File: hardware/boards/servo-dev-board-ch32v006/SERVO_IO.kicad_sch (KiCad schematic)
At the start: 7 parts, among them J4 JST-ZH-H, J5 PIN-V, J6 PIN-V

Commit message: updated LCSC part numbers for all symbols
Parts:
- C14: LCSC C307331 -> C28233
- J4: LCSC (none) -> C265404
- J5: LCSC (none) -> C42431812
- J6: LCSC C485354 -> C66690
- R12: LCSC C25744 -> C17414
- R13: LCSC C25900 -> C17673
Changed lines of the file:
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@@
 			)
 		)
-		(property "LCSC" "C25744"
+		(property "LCSC" "C17414"
 			(at 23.876 85.852 0)
 			(effects
@@
 			)
 		)
+		(property "LCSC" "C265404"
+			(at 43.18 39.37 0)
+			(effects
+				(font
+					(size 1.27 1.27)
+				)
+				(hide yes)
+			)
+		)
 		(pin "3"
 		)
@@
 			)
 		)
-		(property "LCSC" "C307331"
+		(property "LCSC" "C28233"
 			(at 70.866 97.536 0)
 			(effects
@@
 			)
 		)
-		(property "LCSC" "C25900"
+		(property "LCSC" "C17673"
 			(at 64.516 87.63 0)
 			(effects
@@
 			)
 		)
-		(property "LCSC" "C485354"
+		(property "LCSC" "C66690"
 			(at 147.32 40.64 0)
 			(effects
@@
 			(effects
 				(font
+					(size 1.27 1.27)
+				)
+				(hide yes)
+			)
+		)
+		(property "LCSC" "C42431812"
+			(at 96.52 40.64 0)
+			(effects
+				(font

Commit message: remove 'LCSC Part' Property from project
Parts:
- J4: LCSC Part C265404 -> (none)
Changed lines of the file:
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@@
-			)
-		)
-		(property "LCSC Part" "C265404"
-			(at 43.18 68.58 0)
-			(effects
-				(font
-					(size 1.27 1.27)
-				)
-				(hide yes)
 			)
 		)

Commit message: added MFPN properties
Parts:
- C14: MFPN (none) -> CL21B104KCFNNNE
- J4: MFPN (none) -> S5B-ZR(LF)(SN)
- J5: MFPN (none) -> PZ2.54-1X5P-H25
- J6: MFPN (none) -> 2.54-2*2P
- R12: MFPN (none) -> 0805W8F1002T5E
- R13: MFPN (none) -> 0805W8F4701T5E
- TH1: MFPN (none) -> SDNT2012X103F3950FTF
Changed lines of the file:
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@@
+			)
+		)
+		(property "MFPN" "0805W8F1002T5E"
+			(at 23.876 85.852 0)
+			(effects
+				(font
+					(size 1.27 1.27)
+				)
+				(hide yes)
 			)
 		)
@@
 			)
 		)
+		(property "MFPN" "S5B-ZR(LF)(SN)"
+			(at 43.18 39.37 0)
+			(effects
+				(font
+					(size 1.27 1.27)
+				)
+				(hide yes)
+			)
+		)
 		(pin "3"
 		)
@@
 			)
 		)
+		(property "MFPN" "CL21B104KCFNNNE"
+			(at 70.866 97.536 0)
+			(effects
+				(font
+					(size 1.27 1.27)
+				)
+				(hide yes)
+			)
+		)
 		(pin "1"
 		)
@@
 			)
 		)
+		(property "MFPN" "0805W8F4701T5E"
+			(at 64.516 87.63 0)
+			(effects
+				(font
+					(size 1.27 1.27)
+				)
+				(hide yes)
+			)
+		)
 		(pin "1"
 		)
@@
 			)
 		)
+		(property "MFPN" "SDNT2012X103F3950FTF"
+			(at 31.75 97.7899 0)
+			(effects
+				(font
+					(size 1.27 1.27)
+				)
+				(hide yes)
+			)
+		)
 		(pin "2"
 		)
@@
 			)
 		)
+		(property "MFPN" "2.54-2*2P"
+			(at 147.32 40.64 0)
+			(effects
+				(font
+					(size 1.27 1.27)
+				)
+				(hide yes)
+			)
+		)
 		(pin "4"
 		)
@@
 			(at 96.52 40.64 0)
 			(effects
+				(font
+					(size 1.27 1.27)
+				)
+				(hide yes)
+			)
+		)
+		(property "MFPN" "PZ2.54-1X5P-H25"
+			(at 96.52 40.64 0)
+			(effects

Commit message: update board
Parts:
- removed R12: 10kΩ, Resistor_SMD:R_0805_2012Metric_Pad1.20x1.40mm_HandSolder, symbol Device:R
- added J5: NTC EXT, symbol Connector_Generic:Conn_01x02
- added JP1: Jumper_3_Open, symbol Jumper:Jumper_3_Open
- added R13: 10kΩ, Resistor_SMD:R_0805_2012Metric_Pad1.20x1.40mm_HandSolder, symbol Device:R
- renumbered C14 to C11, J5 to J6, J6 to J7, R13 to R14
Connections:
- net +3V3: now also R13.1
- net GND: now also J5.2 (Pin_2)
- net VNTC: now also JP1.2 (C), R13.2; no longer TH1.1
- new net: J5.1 (Pin_1), JP1.1 (A)
- new net: JP1.3 (B), TH1.1
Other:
- moved on the sheet: C11, R14, TH1

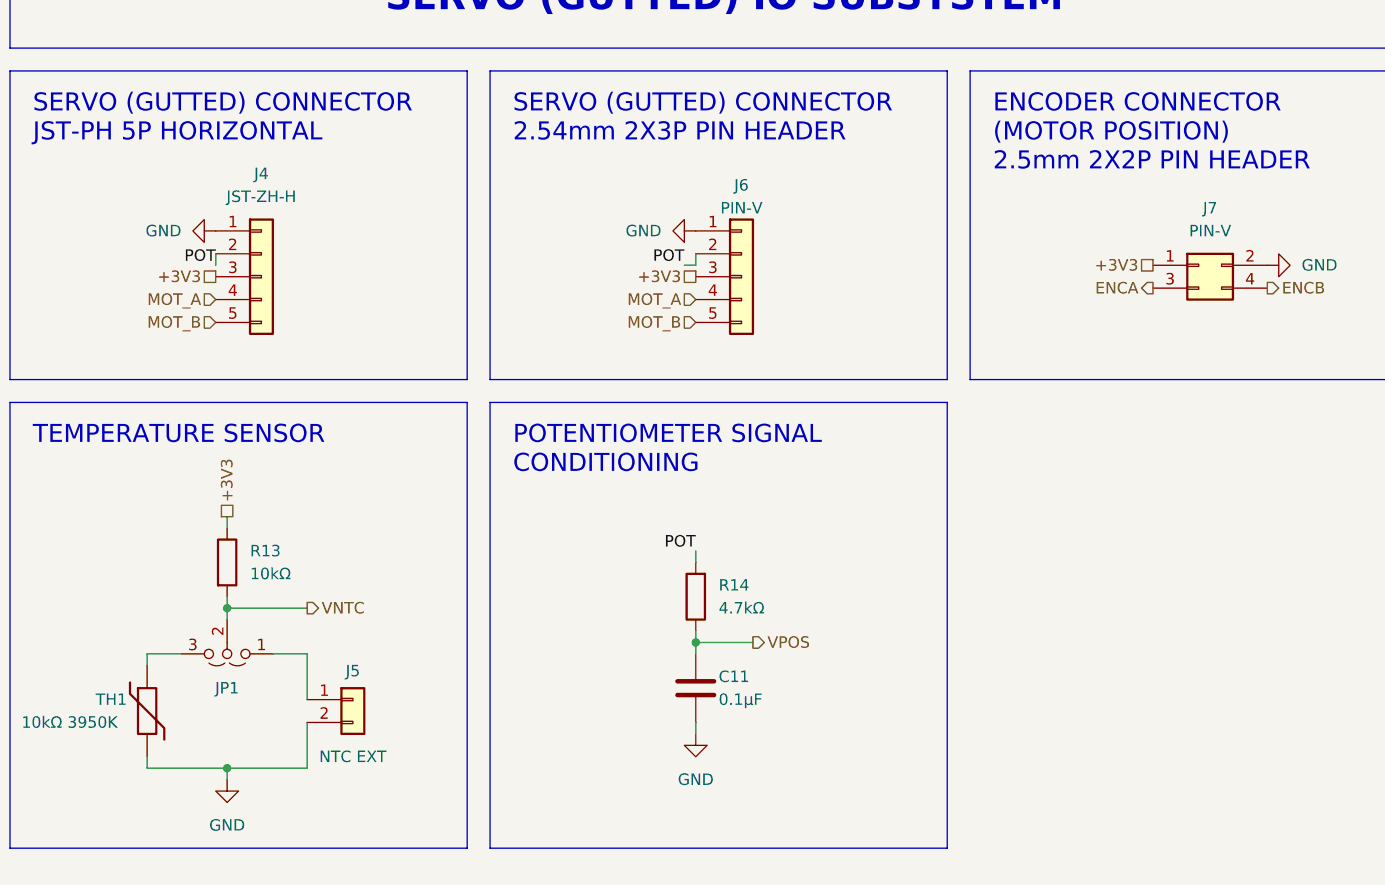
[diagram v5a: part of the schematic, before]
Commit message: updated schematics. ERC on schematics is now passing
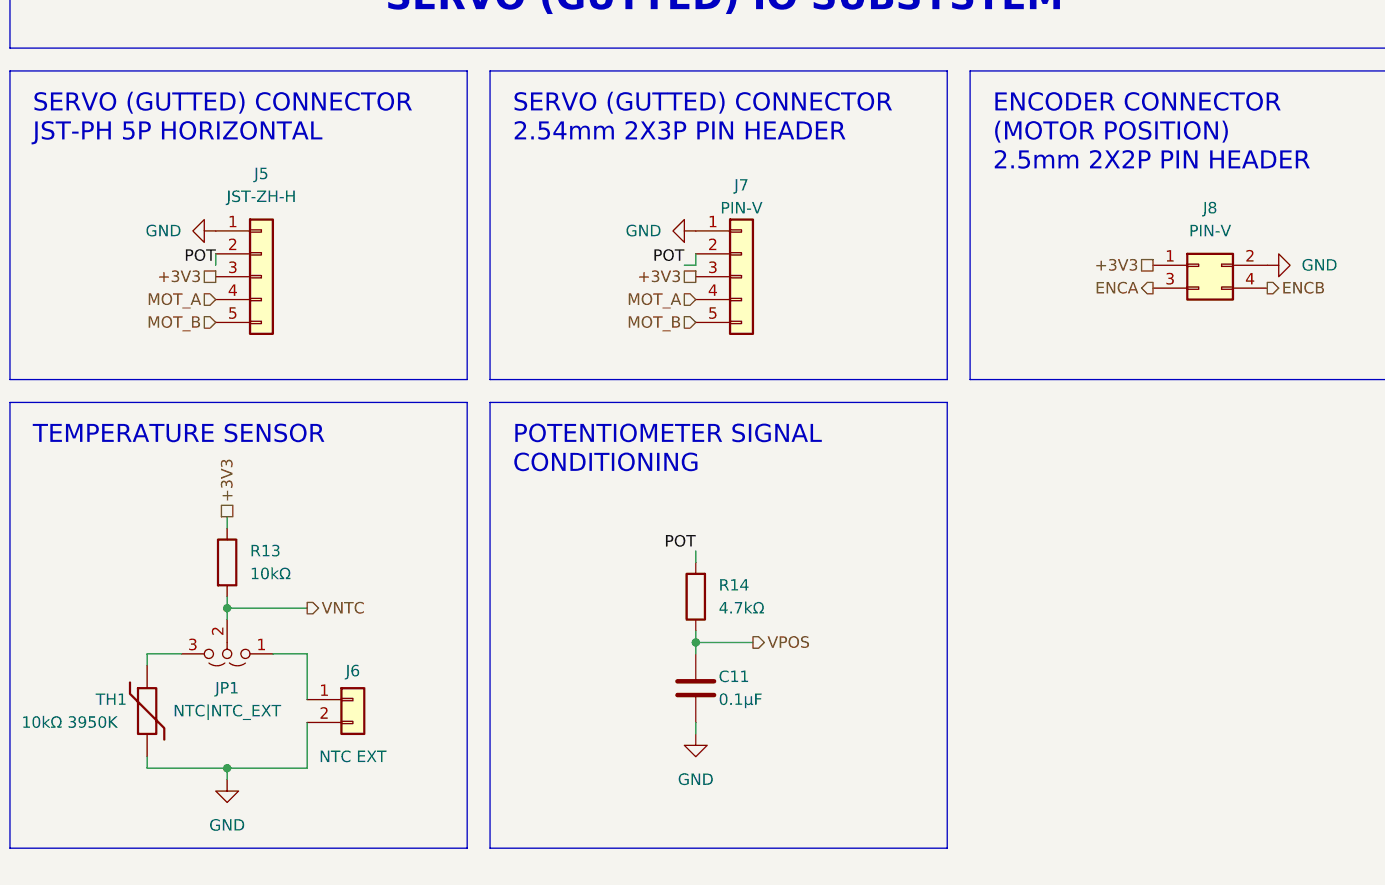
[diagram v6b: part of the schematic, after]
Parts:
- J6: renamed from J5; footprint (none) -> Connector_PinHeader_2.54mm:PinHeader_1x02_P2.54mm_Vertical
- JP1: value Jumper_3_Open -> NTC|NTC_EXT; footprint (none) -> Connector_PinHeader_2.54mm:PinHeader_1x03_P2.54mm_Vertical
- renumbered J4 to J5, J6 to J7, J7 to J8
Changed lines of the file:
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@@
 			)
 		)
-		(property "Value" "Jumper_3_Open"
+		(property "Value" "NTC|NTC_EXT"
 			(at 39.37 99.06 0)
-			(hide yes)
-			(show_name no)
-			(do_not_autoplace no)
-			(effects
-				(font
-					(size 1.27 1.27)
-				)
-			)
-		)
-		(property "Footprint" ""
+			(show_name no)
+			(do_not_autoplace no)
+			(effects
+				(font
+					(size 1.27 1.27)
+				)
+			)
+		)
+		(property "Footprint" "Connector_PinHeader_2.54mm:PinHeader_1x03_P2.54mm_Vertical"
 			(at 39.37 92.71 0)
 			(hide yes)
@@
 		(dnp no)
 		(fields_autoplaced yes)
-		(property "Reference" "#PWR040"
+		(property "Reference" "#PWR046"
 			(at 91.44 107.95 0)
 			(hide yes)
@@
 			(project "servo-dev-board-ch32v006"
 				(path "/6062e7d2-0c72-467e-b49c-6387ba053e09/120e2627-930f-4b00-8e4a-c64cf3d97f18"
-					(reference "#PWR040")
+					(reference "#PWR046")
 					(unit 1)
 				)
@@
 		(in_pos_files yes)
 		(dnp no)
-		(property "Reference" "J4"
+		(property "Reference" "J5"
 			(at 43.18 39.37 0)
 			(show_name no)
@@
 			(project "servo-dev-board-ch32v006"
 				(path "/6062e7d2-0c72-467e-b49c-6387ba053e09/120e2627-930f-4b00-8e4a-c64cf3d97f18"
-					(reference "J4")
+					(reference "J5")
 					(unit 1)
 				)
@@
 		(dnp no)
 		(fields_autoplaced yes)
-		(property "Reference" "#PWR041"
+		(property "Reference" "#PWR047"
 			(at 161.29 49.53 0)
 			(hide yes)
@@
 			(project "servo-dev-board-ch32v006"
 				(path "/6062e7d2-0c72-467e-b49c-6387ba053e09/120e2627-930f-4b00-8e4a-c64cf3d97f18"
-					(reference "#PWR041")
+					(reference "#PWR047")
 					(unit 1)
 				)
@@
 		(dnp no)
 		(fields_autoplaced yes)
-		(property "Reference" "#PWR039"
+		(property "Reference" "#PWR045"
 			(at 85.09 45.72 0)
 			(hide yes)
@@
 			(project "servo-dev-board-ch32v006"
 				(path "/6062e7d2-0c72-467e-b49c-6387ba053e09/120e2627-930f-4b00-8e4a-c64cf3d97f18"
-					(reference "#PWR039")
+					(reference "#PWR045")
 					(unit 1)
 				)
@@
 		(in_pos_files yes)
 		(dnp no)
-		(property "Reference" "J5"
+		(property "Reference" "J6"
 			(at 53.34 94.615 0)
 			(show_name no)
@@
 			)
 		)
-		(property "Footprint" ""
+		(property "Footprint" "Connector_PinHeader_2.54mm:PinHeader_1x02_P2.54mm_Vertical"
 			(at 53.34 97.79 0)
 			(hide yes)
@@
 			(project "servo-dev-board-ch32v006"
 				(path "/6062e7d2-0c72-467e-b49c-6387ba053e09/120e2627-930f-4b00-8e4a-c64cf3d97f18"
-					(reference "J5")
+					(reference "J6")
 					(unit 1)
 				)
@@
 		(dnp no)
 		(fields_autoplaced yes)
-		(property "Reference" "#PWR037"
+		(property "Reference" "#PWR043"
 			(at 31.75 45.72 0)
 			(hide yes)
@@
 			(project "servo-dev-board-ch32v006"
 				(path "/6062e7d2-0c72-467e-b49c-6387ba053e09/120e2627-930f-4b00-8e4a-c64cf3d97f18"
-					(reference "#PWR037")
+					(reference "#PWR043")
 					(unit 1)
 				)
@@
 		(in_pos_files yes)
 		(dnp no)
-		(property "Reference" "#PWR038"
+		(property "Reference" "#PWR044"
 			(at 39.37 113.03 0)
 			(hide yes)
@@
 			(project "servo-dev-board-ch32v006"
 				(path "/6062e7d2-0c72-467e-b49c-6387ba053e09/120e2627-930f-4b00-8e4a-c64cf3d97f18"
-					(reference "#PWR038")
+					(reference "#PWR044")
 					(unit 1)
 				)
@@
 		(in_pos_files yes)
 		(dnp no)
-		(property "Reference" "J7"
+		(property "Reference" "J8"
 			(at 148.59 43.18 0)
 			(show_name no)
@@
 			(project "servo-dev-board-ch32v006"
 				(path "/6062e7d2-0c72-467e-b49c-6387ba053e09/120e2627-930f-4b00-8e4a-c64cf3d97f18"
-					(reference "J7")
+					(reference "J8")
 					(unit 1)
 				)
@@
 		(in_pos_files yes)
 		(dnp no)
-		(property "Reference" "J6"
+		(property "Reference" "J7"
 			(at 96.52 40.64 0)
 			(show_name no)
@@
 			(project "servo-dev-board-ch32v006"
 				(path "/6062e7d2-0c72-467e-b49c-6387ba053e09/120e2627-930f-4b00-8e4a-c64cf3d97f18"
-					(reference "J6")
-					(unit 1)
-				)
+					(reference "J7")
+					(unit 1)
+				)

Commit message: completed routing.
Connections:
- net VNTC_EXT: now reaches J6.1 (Pin_1), JP1.1 (A)
- net VNTC_INT: now reaches JP1.3 (B), TH1.1
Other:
- moved on the sheet: C11, J6, JP1, R13, R14, TH1
